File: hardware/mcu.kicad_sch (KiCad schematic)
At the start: 1 part

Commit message: Start new schematics
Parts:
- added B1: Reset, symbol Switch:SW_MEC_5E
- added C17: 100 nF, symbol Device:C
- added C2: 10uF, symbol Device:C
- added C3_25, C3_36, C3_48, C5_9: 100nF, symbol Device:C
- added C4: 1uF, symbol Device:C
- added D0: D_Zener, symbol Device:D_Zener
- added JP0: Bootloader, symbol Jumper:SolderJumper_2_Open
- added JP1: Bootflash, symbol Jumper:SolderJumper_2_Open
- added JP2: RESETB_NRST, symbol Jumper:SolderJumper_2_Open
- U0: renamed from U?; value (none) -> STM32U575CIU6Q; footprint (none) -> KnxBoard:STM32U575CIU6Q
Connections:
- net NRST: now also B1.1, B1.2, C17.1, D0.1 (K), JP2.1 (A)
- net +3.3V: now reaches U0.1 (VBAT)
- net +3.3V: now also U0.25 (VDD), U0.36 (VDD), U0.48 (VDD), U0.9 (VDDA), C2.1, C3_25.1, C3_36.1, C3_48.1, C4.1, C5_9.1, JP0.2 (B)
- net KNX_PROG_LED: now reaches U0.2 (PC13)
- net GNDREF: now reaches U0.22 (VSSSMPS)
- net GNDREF: now also U0.24 (VSS), U0.35 (VSS), U0.47 (VSS), U0.49 (EPAD), U0.8 (VSSA), B1.3 (K), B1.4 (A), C17.2, C2.2, C3_25.2, C3_36.2, C3_48.2, C4.2, C5_9.2, D0.2 (A), JP1.1 (A)
- net KNX_PROG_BTN: now reaches U0.3 (PC14-OSC32_IN)
- net KNX_SAVEB: now reaches U0.4 (PC15-OSC32_OUT)
- net at U0.44 (PH3-BOOT0): now also JP0.1 (A), JP1.2 (B)
- net KNX_RESETB: now reaches U0.6 (PH1-OSC_OUT)
- net KNX_RESETB: now also JP2.2 (B)
- no-connect marks 0 -> 4

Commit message: Work in progress
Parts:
- B1: footprint (none) -> Button_Switch_SMD:SW_SPST_SKQG_WithStem
- C1: renamed from C17; footprint (none) -> Capacitor_SMD:C_0603_1608Metric_Pad1.08x0.95mm_HandSolder
- C2, C3_25, C3_36, C3_48, C4, C5_9: footprint (none) -> Capacitor_SMD:C_0603_1608Metric_Pad1.08x0.95mm_HandSolder
- D0: footprint (none) -> Diode_SMD:D_SOD-323
- JP0, JP1, JP2: footprint (none) -> Jumper:SolderJumper-2_P1.3mm_Open_TrianglePad1.0x1.5mm
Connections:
- net PA0: now reaches U0.10 (PA0)
- net PA1: now reaches U0.11 (PA1)
- net PA4: now reaches U0.14 (PA4)
- net PA5: now reaches U0.15 (PA5)
- net PA6: now reaches U0.16 (PA6)
- net PA7: now reaches U0.17 (PA7)
- net PB0: now reaches U0.18 (PB0)
- net PB1: now reaches U0.19 (PB1)
- net PB13: now reaches U0.26 (PB13)
- net PB14: now reaches U0.27 (PB14)
- net PB15: now reaches U0.28 (PB15)
- net PA8: now reaches U0.29 (PA8)
- net PA11: now reaches U0.32 (PA11)
- net PA12: now reaches U0.33 (PA12)
- net PB4: now reaches U0.40 (PB4)
- net PB5: now reaches U0.41 (PB5)
- net PB6: now reaches U0.42 (PB6)
- net PB7: now reaches U0.43 (PB7)
- net PB8: now reaches U0.45 (PB8)
- net +3.3V renamed VDD

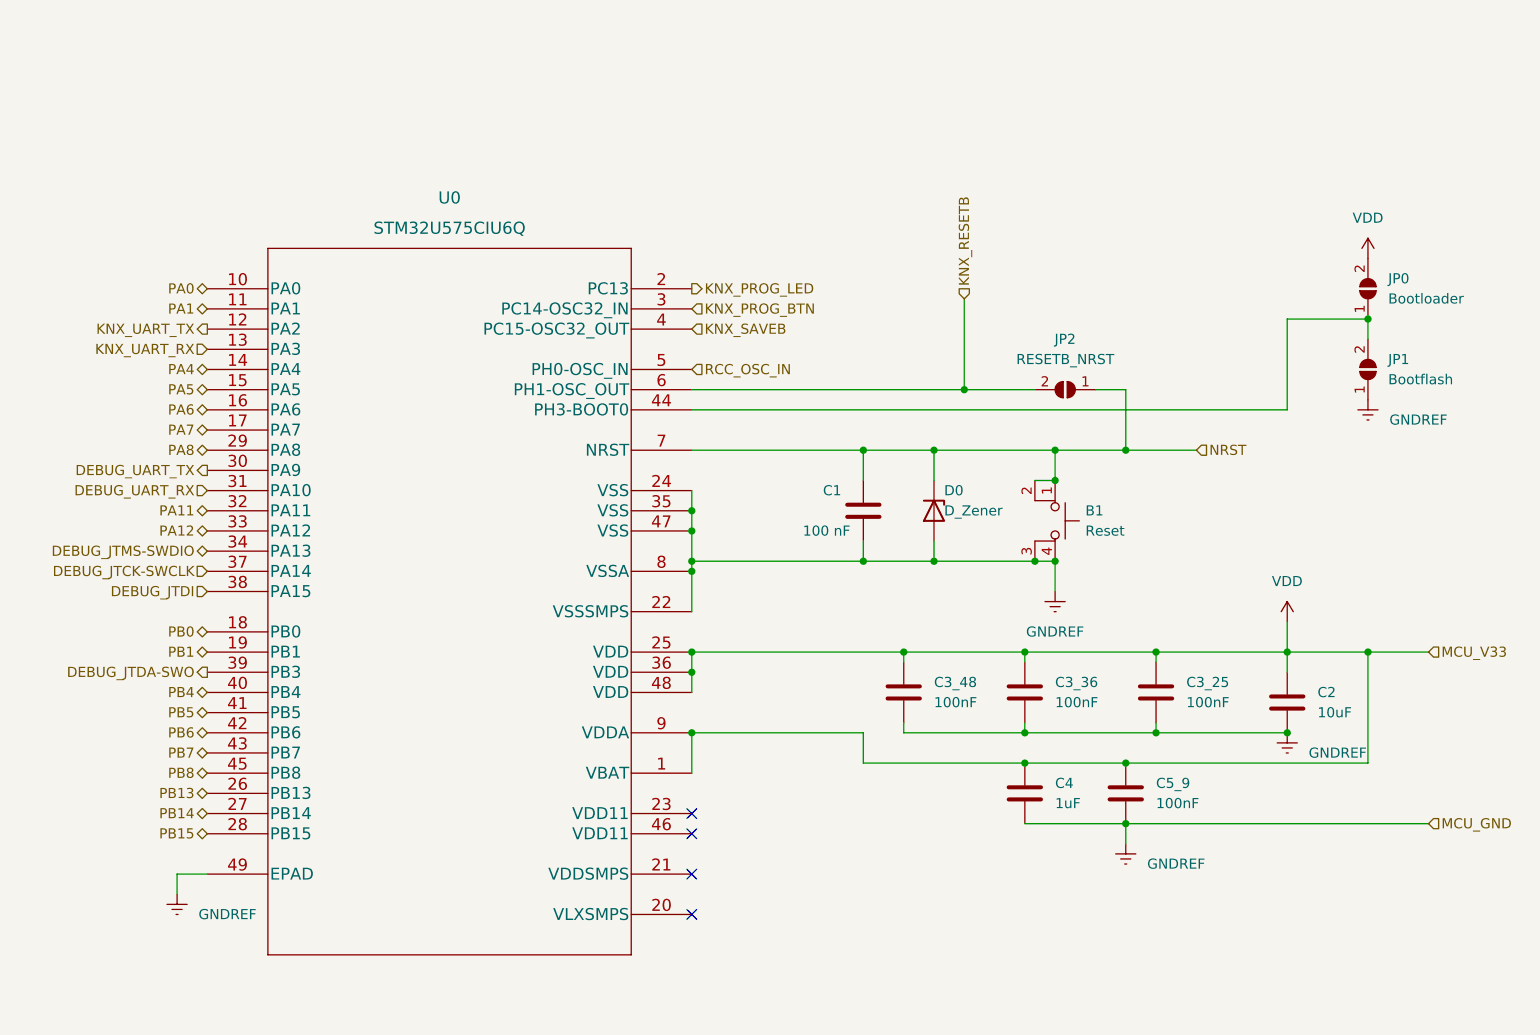
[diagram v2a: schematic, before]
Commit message: Switch to STM32U575CIT6
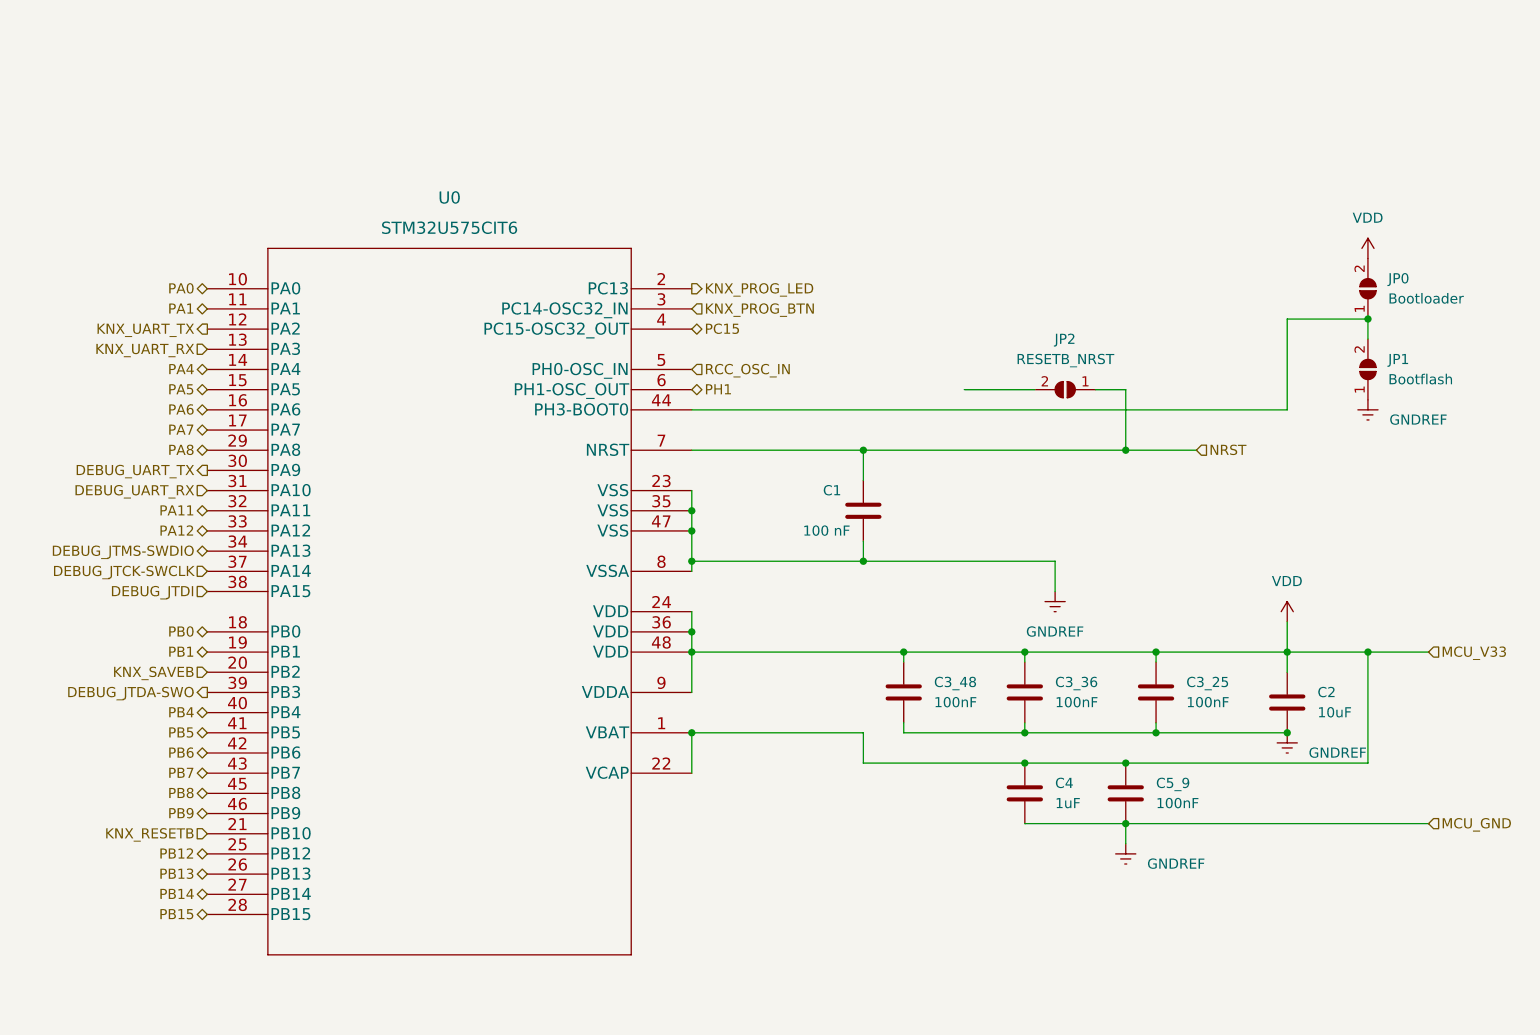
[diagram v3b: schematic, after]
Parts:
- removed B1: Reset, Button_Switch_SMD:SW_SPST_SKQG_WithStem, symbol Switch:SW_MEC_5E
- removed D0: D_Zener, Diode_SMD:D_SOD-323, symbol Device:D_Zener
- removed U0: STM32U575CIU6Q, KnxBoard:STM32U575CIU6Q, symbol STM32U:STM32U575CIU6Q
- added U0: STM32U575CIT6, KnxBoard:STM32U575CIT6, symbol STM32U575CIT6:STM32U575CIT6
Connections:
- net DEBUG_JTCK-SWCLK: now also U0.37 (PA14)
- net DEBUG_JTDA-SWO: now also U0.39 (PB3)
- net DEBUG_JTDI: now also U0.38 (PA15)
- net DEBUG_JTMS-SWDIO: now also U0.34 (PA13)
- net DEBUG_UART_RX: now also U0.31 (PA10)
- net DEBUG_UART_TX: now also U0.30 (PA9)
- net GNDREF: now also U0.23 (VSS), U0.35 (VSS), U0.47 (VSS), U0.8 (VSSA)
- net KNX_PROG_BTN: now also U0.3 (PC14-OSC32_IN)
- net KNX_PROG_LED: now also U0.2 (PC13)
- net KNX_RESETB: now also U0.21 (PB10); no longer JP2.2 (B)
- net KNX_SAVEB: now also U0.20 (PB2)
- net KNX_UART_RX: now also U0.13 (PA3)
- net KNX_UART_TX: now also U0.12 (PA2)
- net NRST: now also U0.7 (NRST)
- net PA0: now also U0.10 (PA0)
- net PA1: now also U0.11 (PA1)
- net PA11: now also U0.32 (PA11)
- net PA12: now also U0.33 (PA12)
- net PA4: now also U0.14 (PA4)
- net PA5: now also U0.15 (PA5)
- net PA6: now also U0.16 (PA6)
- net PA7: now also U0.17 (PA7)
- net PA8: now also U0.29 (PA8)
- net PB0: now also U0.18 (PB0)
- net PB1: now also U0.19 (PB1)
- net PB13: now also U0.26 (PB13)
- net PB14: now also U0.27 (PB14)
- net PB15: now also U0.28 (PB15)
- net PB4: now also U0.40 (PB4)
- net PB5: now also U0.41 (PB5)
- net PB6: now also U0.42 (PB6)
- net PB7: now also U0.43 (PB7)
- net PB8: now also U0.45 (PB8)
- net RCC_OSC_IN: now also U0.5 (PH0-OSC_IN)
- net VDD: now also U0.1 (VBAT), U0.22 (VCAP), U0.24 (VDD), U0.36 (VDD), U0.48 (VDD), U0.9 (VDDA)
- net at JP0.1 (A), JP1.2 (B): now also U0.44 (PH3-BOOT0)
- new net PB12: U0.25 (PB12)
- new net PB9: U0.46 (PB9)
- new net PC15: U0.4 (PC15-OSC32_OUT)
- new net PH1: U0.6 (PH1-OSC_OUT)
- no-connect marks 4 -> 0

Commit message: Progress
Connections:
- net KNX_RESETB: now also JP2.2 (B)
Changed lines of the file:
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@@
     (effects (font (size 1.27 1.27)) (justify right))
   )
-  (hierarchical_label "MCU_V33" (shape input) (at 259.08 100.33 0)
-    (effects (font (size 1.27 1.27)) (justify left))
-  )
-  (hierarchical_label "MCU_GND" (shape input) (at 259.08 121.92 0)
+  (hierarchical_label "VDD" (shape input) (at 259.08 100.33 0)
+    (effects (font (size 1.27 1.27)) (justify left))
+  )
+  (hierarchical_label "GNDREF" (shape input) (at 259.08 121.92 0)
     (effects (font (size 1.27 1.27)) (justify left))
   )
@@
   )
   (hierarchical_label "DEBUG_JTDA-SWO" (shape output) (at 105.41 105.41 180)
+    (effects (font (size 1.27 1.27)) (justify right))
+  )
+  (hierarchical_label "KNX_RESETB" (shape input) (at 200.66 67.31 180)
     (effects (font (size 1.27 1.27)) (justify right))
   )
@@
     (pin "2")
   )
-  (symbol (lib_id "power:VDD") (at 241.3 96.52 0) (unit 1)
-    (in_bom yes) (on_board yes) (fields_autoplaced)
-    (property "Reference" "#PWR0109" (id 0) (at 241.3 100.33 0)
-      (effects (font (size 1.27 1.27)) hide)
-    )
-    (property "Value" "VDD" (id 1) (at 241.3 91.44 0))
-    (property "Footprint" "" (id 2) (at 241.3 96.52 0)
-      (effects (font (size 1.27 1.27)) hide)
-    )
-    (property "Datasheet" "" (id 3) (at 241.3 96.52 0)
-      (effects (font (size 1.27 1.27)) hide)
-    )
-    (pin "1")
-  )
   (symbol (lib_id "Device:C") (at 187.96 82.55 0) (unit 1)
     (in_bom yes) (on_board yes)
@@
     (pin "1")
   )
+  (symbol (lib_id "power:GNDREF") (at 212.09 92.71 0) (unit 1)
+    (in_bom yes) (on_board yes) (fields_autoplaced)
+    (property "Reference" "#PWR0114" (id 0) (at 212.09 99.06 0)
+      (effects (font (size 1.27 1.27)) hide)
+    )
+    (property "Value" "GNDREF" (id 1) (at 212.09 97.79 0))
+    (property "Footprint" "" (id 2) (at 212.09 92.71 0)
+      (effects (font (size 1.27 1.27)) hide)
+    )
+    (property "Datasheet" "" (id 3) (at 212.09 92.71 0)
+      (effects (font (size 1.27 1.27)) hide)
+    )
+    (pin "1")
+  )
+  (symbol (lib_id "Device:C") (at 224.79 105.41 0) (unit 1)
+    (in_bom yes) (on_board yes) (fields_autoplaced)
+    (property "Reference" "C3_25" (id 0) (at 228.6 104.1399 0)
+      (effects (font (size 1.27 1.27)) (justify left))
+    )
+    (property "Value" "100nF" (id 1) (at 228.6 106.6799 0)
+      (effects (font (size 1.27 1.27)) (justify left))
+    )
+    (property "Footprint" "Capacitor_SMD:C_0603_1608Metric_Pad1.08x0.95mm_HandSolder" (id 2) (at 225.7552 109.22 0)
+      (effects (font (size 1.27 1.27)) hide)
+    )
+    (property "Datasheet" "~" (id 3) (at 224.79 105.41 0)
+      (effects (font (size 1.27 1.27)) hide)
+    )
+    (pin "1")
+    (pin "2")
+  )
+  (symbol (lib_id "Device:C") (at 241.3 106.68 0) (unit 1)
+    (in_bom yes) (on_board yes) (fields_autoplaced)
+    (property "Reference" "C2" (id 0) (at 245.11 105.4099 0)
+      (effects (font (size 1.27 1.27)) (justify left))
+    )
+    (property "Value" "10uF" (id 1) (at 245.11 107.9499 0)
+      (effects (font (size 1.27 1.27)) (justify left))
+    )
+    (property "Footprint" "Capacitor_SMD:C_0603_1608Metric_Pad1.08x0.95mm_HandSolder" (id 2) (at 242.2652 110.49 0)
+      (effects (font (size 1.27 1.27)) hide)
+    )
+    (property "Datasheet" "~" (id 3) (at 241.3 106.68 0)
+      (effects (font (size 1.27 1.27)) hide)
+    )
+    (pin "1")
+    (pin "2")
+  )
+  (symbol (lib_id "Device:C") (at 193.04 105.41 0) (unit 1)
+    (in_bom yes) (on_board yes) (fields_autoplaced)
+    (property "Reference" "C3_48" (id 0) (at 196.85 104.1399 0)
+      (effects (font (size 1.27 1.27)) (justify left))
+    )
+    (property "Value" "100nF" (id 1) (at 196.85 106.6799 0)
+      (effects (font (size 1.27 1.27)) (justify left))
+    )
+    (property "Footprint" "Capacitor_SMD:C_0603_1608Metric_Pad1.08x0.95mm_HandSolder" (id 2) (at 194.0052 109.22 0)
+      (effects (font (size 1.27 1.27)) hide)
+    )
+    (property "Datasheet" "~" (id 3) (at 193.04 105.41 0)
+      (effects (font (size 1.27 1.27)) hide)
+    )
+    (pin "1")
+    (pin "2")
+  )
   (symbol (lib_id "power:VDD") (at 251.46 50.8 0) (unit 1)
     (in_bom yes) (on_board yes) (fields_autoplaced)
-    (property "Reference" "#PWR0112" (id 0) (at 251.46 54.61 0)
+    (property "Reference" "#PWR0113" (id 0) (at 251.46 54.61 0)
       (effects (font (size 1.27 1.27)) hide)
     )
@@
     (pin "1")
   )
-  (symbol (lib_id "power:GNDREF") (at 212.09 92.71 0) (unit 1)
-    (in_bom yes) (on_board yes) (fields_autoplaced)
-    (property "Reference" "#PWR0114" (id 0) (at 212.09 99.06 0)
-      (effects (font (size 1.27 1.27)) hide)
-    )
-    (property "Value" "GNDREF" (id 1) (at 212.09 97.79 0))
-    (property "Footprint" "" (id 2) (at 212.09 92.71 0)
-      (effects (font (size 1.27 1.27)) hide)
-    )
-    (property "Datasheet" "" (id 3) (at 212.09 92.71 0)
-      (effects (font (size 1.27 1.27)) hide)
-    )
-    (pin "1")
-  )
-  (symbol (lib_id "Device:C") (at 224.79 105.41 0) (unit 1)
-    (in_bom yes) (on_board yes) (fields_autoplaced)
-    (property "Reference" "C3_25" (id 0) (at 228.6 104.1399 0)
-      (effects (font (size 1.27 1.27)) (justify left))
-    )
-    (property "Value" "100nF" (id 1) (at 228.6 106.6799 0)
-      (effects (font (size 1.27 1.27)) (justify left))
-    )
-    (property "Footprint" "Capacitor_SMD:C_0603_1608Metric_Pad1.08x0.95mm_HandSolder" (id 2) (at 225.7552 109.22 0)
-      (effects (font (size 1.27 1.27)) hide)
-    )
-    (property "Datasheet" "~" (id 3) (at 224.79 105.41 0)
-      (effects (font (size 1.27 1.27)) hide)
-    )
-    (pin "1")
-    (pin "2")
-  )
-  (symbol (lib_id "Device:C") (at 241.3 106.68 0) (unit 1)
-    (in_bom yes) (on_board yes) (fields_autoplaced)
-    (property "Reference" "C2" (id 0) (at 245.11 105.4099 0)
-      (effects (font (size 1.27 1.27)) (justify left))
-    )
-    (property "Value" "10uF" (id 1) (at 245.11 107.9499 0)
-      (effects (font (size 1.27 1.27)) (justify left))
-    )
-    (property "Footprint" "Capacitor_SMD:C_0603_1608Metric_Pad1.08x0.95mm_HandSolder" (id 2) (at 242.2652 110.49 0)
-      (effects (font (size 1.27 1.27)) hide)
-    )
-    (property "Datasheet" "~" (id 3) (at 241.3 106.68 0)
-      (effects (font (size 1.27 1.27)) hide)
-    )
-    (pin "1")
-    (pin "2")
-  )
-  (symbol (lib_id "Device:C") (at 193.04 105.41 0) (unit 1)
-    (in_bom yes) (on_board yes) (fields_autoplaced)
-    (property "Reference" "C3_48" (id 0) (at 196.85 104.1399 0)
-      (effects (font (size 1.27 1.27)) (justify left))
-    )
-    (property "Value" "100nF" (id 1) (at 196.85 106.6799 0)
-      (effects (font (size 1.27 1.27)) (justify left))
-    )
-    (property "Footprint" "Capacitor_SMD:C_0603_1608Metric_Pad1.08x0.95mm_HandSolder" (id 2) (at 194.0052 109.22 0)
-      (effects (font (size 1.27 1.27)) hide)
-    )
-    (property "Datasheet" "~" (id 3) (at 193.04 105.41 0)
-      (effects (font (size 1.27 1.27)) hide)
-    )
-    (pin "1")
-    (pin "2")
+  (symbol (lib_id "power:VDD") (at 241.3 96.52 0) (unit 1)
+    (in_bom yes) (on_board yes) (fields_autoplaced)
+    (property "Reference" "#PWR0112" (id 0) (at 241.3 100.33 0)
+      (effects (font (size 1.27 1.27)) hide)
+    )
+    (property "Value" "VDD" (id 1) (at 241.3 91.44 0))
+    (property "Footprint" "" (id 2) (at 241.3 96.52 0)
+      (effects (font (size 1.27 1.27)) hide)
+    )
+    (property "Datasheet" "" (id 3) (at 241.3 96.52 0)
+      (effects (font (size 1.27 1.27)) hide)
+    )
+    (pin "1")
   )
   (symbol (lib_id "Jumper:SolderJumper_2_Open") (at 213.36 67.31 180) (unit 1)
